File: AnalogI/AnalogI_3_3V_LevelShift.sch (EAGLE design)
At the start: 80 parts, among them IC1 HCPL-7800, IC2 HCPL-7800, IC3 HCPL-7800, IC4 HCPL-7800, IC5 MCP3424SOIC, IC6 74HC4051_MUXN, IC7 74HC4051_MUXN, P1 DF11-06-2DSA, Q1 BS170, Q2 BS170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

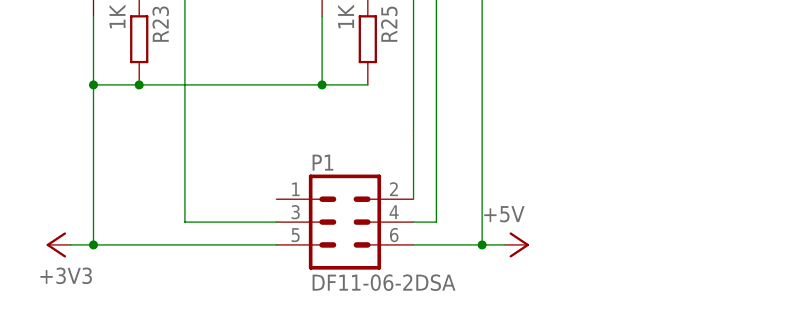
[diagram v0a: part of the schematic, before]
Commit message: Change connector. Modified solder mask.
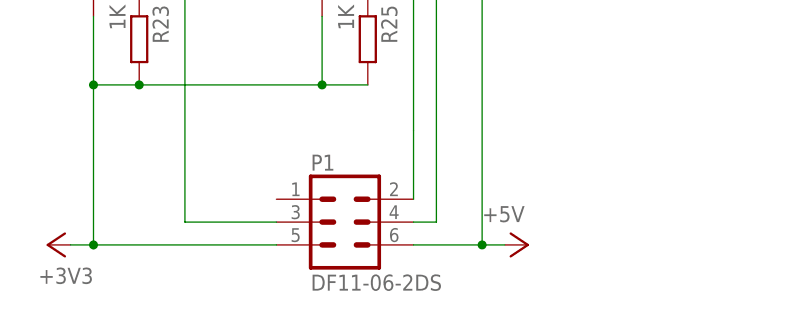
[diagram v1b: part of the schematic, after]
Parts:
- P1: value DF11-06-2DSA -> DF11-06-2DS; device con-hirose-df11:DF11-06-2DSA -> con-hirose-df11:DF11-06-2DS
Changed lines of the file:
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@@
 </part>
 <part name="+3V2" library="supply1" deviceset="+3V3" device=""/>
-<part name="P1" library="con-hirose-df11" deviceset="DF11-06-2DSA" device="">
+<part name="P1" library="con-hirose-df11" deviceset="DF11-06-2" device="DS">
 <attribute name="MF" value=""/>
 <attribute name="MPN" value=""/>

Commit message: Move DC/DC coppler. Update Gerbers.
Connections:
- net N$33 renamed AGND
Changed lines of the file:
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@@
 </segment>
 </net>
-<net name="N$33" class="0">
+<net name="AGND" class="0">
 <segment>
 <pinref part="C8" gate="G$1" pin="2"/>

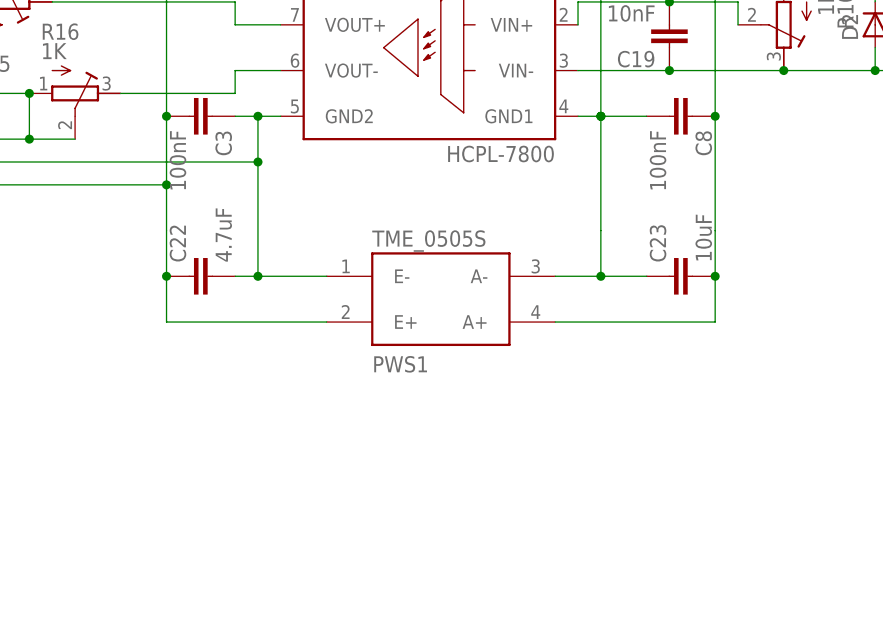
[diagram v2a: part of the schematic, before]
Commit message: Add load resistor.
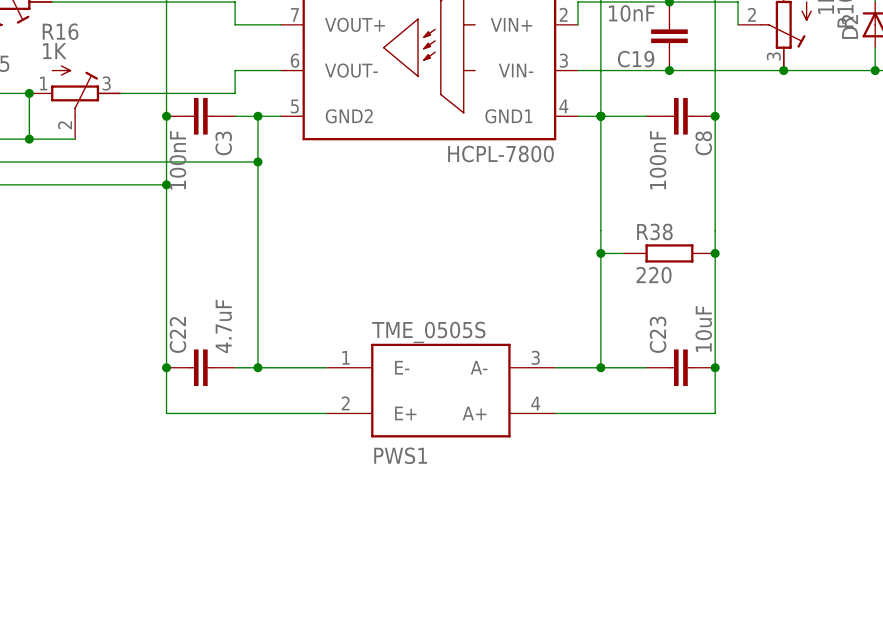
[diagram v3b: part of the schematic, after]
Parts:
- added R38: 220, rcl:R-EU_0204/2V
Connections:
- net AGND: now also R38.1
- net N$8: now also R38.2
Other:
- moved on the sheet: C22, C23, PWS1
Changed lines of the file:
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@@
 <part name="C23" library="rcl" deviceset="C-EU" device="C0805" value="10uF"/>
 <part name="C22" library="rcl" deviceset="C-EU" device="C0805" value="4.7uF"/>
+<part name="R38" library="rcl" deviceset="R-EU_" device="0204/2V" value="220"/>
 </parts>
 <sheets>
@@
 <instance part="X1" gate="G$1" x="246.38" y="17.78" rot="MR180"/>
 <instance part="X2" gate="G$1" x="-101.6" y="17.78" rot="R180"/>
-<instance part="PWS1" gate="G$1" x="177.8" y="-25.4" rot="MR180"/>
+<instance part="PWS1" gate="G$1" x="177.8" y="-35.56" rot="MR180"/>
 <instance part="R29" gate="G$1" x="48.26" y="5.08" rot="MR0"/>
 <instance part="R30" gate="G$1" x="53.34" y="0" rot="MR0"/>
@@
 <instance part="R36" gate="G$1" x="-73.66" y="43.18" rot="MR180"/>
 <instance part="R37" gate="G$1" x="-73.66" y="15.24" rot="MR180"/>
-<instance part="C23" gate="G$1" x="203.2" y="-22.86" rot="R90"/>
-<instance part="C22" gate="G$1" x="149.86" y="-22.86" rot="R90"/>
+<instance part="C23" gate="G$1" x="203.2" y="-33.02" rot="R90"/>
+<instance part="C22" gate="G$1" x="149.86" y="-33.02" rot="R90"/>
+<instance part="R38" gate="G$1" x="203.2" y="-20.32"/>
 </instances>
 <busses>
@@
 <junction x="104.14" y="-7.62"/>
 <wire x1="104.14" y1="0" x2="104.14" y2="-7.62" width="0.1524" layer="91"/>
-<wire x1="157.48" y1="-10.16" x2="157.48" y2="-22.86" width="0.1524" layer="91"/>
+<wire x1="157.48" y1="-10.16" x2="157.48" y2="-33.02" width="0.1524" layer="91"/>
 <pinref part="PWS1" gate="G$1" pin="E-"/>
-<wire x1="157.48" y1="-22.86" x2="165.1" y2="-22.86" width="0.1524" layer="91"/>
+<wire x1="157.48" y1="-33.02" x2="165.1" y2="-33.02" width="0.1524" layer="91"/>
 <junction x="157.48" y="-10.16"/>
 <pinref part="IC7" gate="G$1" pin="INH"/>
@@
 <junction x="104.14" y="0"/>
 <pinref part="C22" gate="G$1" pin="2"/>
-<wire x1="157.48" y1="-22.86" x2="154.94" y2="-22.86" width="0.1524" layer="91"/>
-<junction x="157.48" y="-22.86"/>
+<wire x1="157.48" y1="-33.02" x2="154.94" y2="-33.02" width="0.1524" layer="91"/>
+<junction x="157.48" y="-33.02"/>
 </segment>
 </net>
@@
 <wire x1="147.32" y1="-12.7" x2="147.32" y2="-17.78" width="0.1524" layer="91"/>
 <pinref part="PWS1" gate="G$1" pin="E+"/>
-<wire x1="147.32" y1="-17.78" x2="147.32" y2="-22.86" width="0.1524" layer="91"/>
-<wire x1="147.32" y1="-22.86" x2="147.32" y2="-27.94" width="0.1524" layer="91"/>
-<wire x1="147.32" y1="-27.94" x2="165.1" y2="-27.94" width="0.1524" layer="91"/>
+<wire x1="147.32" y1="-17.78" x2="147.32" y2="-33.02" width="0.1524" layer="91"/>
+<wire x1="147.32" y1="-33.02" x2="147.32" y2="-38.1" width="0.1524" layer="91"/>
+<wire x1="147.32" y1="-38.1" x2="165.1" y2="-38.1" width="0.1524" layer="91"/>
 <junction x="147.32" y="-12.7"/>
 <wire x1="0" y1="-12.7" x2="-33.02" y2="-12.7" width="0.1524" layer="91"/>
@@
 <junction x="91.44" y="-27.94"/>
 <pinref part="C22" gate="G$1" pin="1"/>
-<junction x="147.32" y="-22.86"/>
+<junction x="147.32" y="-33.02"/>
 </segment>
 </net>
@@
 <junction x="208.28" y="38.1"/>
 <pinref part="PWS1" gate="G$1" pin="A+"/>
-<wire x1="190.5" y1="-27.94" x2="208.28" y2="-27.94" width="0.1524" layer="91"/>
-<wire x1="208.28" y1="-27.94" x2="208.28" y2="-22.86" width="0.1524" layer="91"/>
+<wire x1="190.5" y1="-38.1" x2="208.28" y2="-38.1" width="0.1524" layer="91"/>
+<wire x1="208.28" y1="-38.1" x2="208.28" y2="-33.02" width="0.1524" layer="91"/>
 <junction x="208.28" y="-5.08"/>
-<wire x1="208.28" y1="-22.86" x2="208.28" y2="-17.78" width="0.1524" layer="91"/>
+<wire x1="208.28" y1="-33.02" x2="208.28" y2="-20.32" width="0.1524" layer="91"/>
+<wire x1="208.28" y1="-20.32" x2="208.28" y2="-17.78" width="0.1524" layer="91"/>
 <wire x1="208.28" y1="-17.78" x2="208.28" y2="-5.08" width="0.1524" layer="91"/>
 <pinref part="C23" gate="G$1" pin="2"/>
-<junction x="208.28" y="-22.86"/>
+<junction x="208.28" y="-33.02"/>
+<pinref part="R38" gate="G$1" pin="2"/>
+<junction x="208.28" y="-20.32"/>
 </segment>
 </net>
@@
 <wire x1="193.04" y1="-5.08" x2="195.58" y2="-5.08" width="0.1524" layer="91"/>
 <pinref part="PWS1" gate="G$1" pin="A-"/>
-<wire x1="190.5" y1="-22.86" x2="195.58" y2="-22.86" width="0.1524" layer="91"/>
-<wire x1="195.58" y1="-22.86" x2="195.58" y2="-17.78" width="0.1524" layer="91"/>
+<wire x1="190.5" y1="-33.02" x2="195.58" y2="-33.02" width="0.1524" layer="91"/>
+<wire x1="195.58" y1="-33.02" x2="195.58" y2="-20.32" width="0.1524" layer="91"/>
 <junction x="195.58" y="-5.08"/>
 <pinref part="C9" gate="G$1" pin="2"/>
 <pinref part="IC1" gate="G$1" pin="GND1"/>
+<wire x1="195.58" y1="-20.32" x2="195.58" y2="-17.78" width="0.1524" layer="91"/>
 <wire x1="195.58" y1="-17.78" x2="195.58" y2="-5.08" width="0.1524" layer="91"/>
 <wire x1="195.58" y1="22.86" x2="200.66" y2="22.86" width="0.1524" layer="91"/>
@@
 <junction x="-48.26" y="-5.08"/>
 <pinref part="C23" gate="G$1" pin="1"/>
-<wire x1="195.58" y1="-22.86" x2="200.66" y2="-22.86" width="0.1524" layer="91"/>
-<junction x="195.58" y="-22.86"/>
-</segment>
-</net>
+<wire x1="195.58" y1="-33.02" x2="200.66" y2="-33.02" width="0.1524" layer="91"/>
+<junction x="195.58" y="-33.02"/>
+<junction x="195.58" y="-20.32"/>
+<pinref part="R38" gate="G$1" pin="1"/>
+<wire x1="195.58" y1="-20.32" x2="198.12" y2="-20.32" width="0.1524" layer="91"/>
+</segment>
+</net>
